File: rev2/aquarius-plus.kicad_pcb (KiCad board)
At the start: 2 copper layers, 167 x 115 mm, 173 parts, among them J1 Power in, J10 FPGA spare, J11 Hand controller 2, J12 Hand controller 1, J13 ESP32 spare, J2 ESP USB Host, J3 Audio out, J4 VGA, J5 Cassette out, J6 Cassette in, J7 Expansion port, J8 Printer, J9 TF-03A, Q1 BC847C, Q2 BC847C, Q3 2N7002, SW1 SW_DPDT_x2, U1 SN74AHCT1G125DBVR, U10 ESP32-S3-WROOM-1-N4R2, U11 LDL1117S33R, U12 SN74CB3T3245PWR, U13 IS61C5128AS-25QLI, U2 SN74AHCT1G125DBVR, U3 LD1117S12, U4 SN74CB3T3245PWR, U5 MAX3221ECPWR, U6 XC6SLX9-2TQG144C, U7 Z84C0010AEG, U8 SN74CB3T3245PWR, U9 SN74CB3T3245PWR, X1 SX3M14.31818M20F30TNN

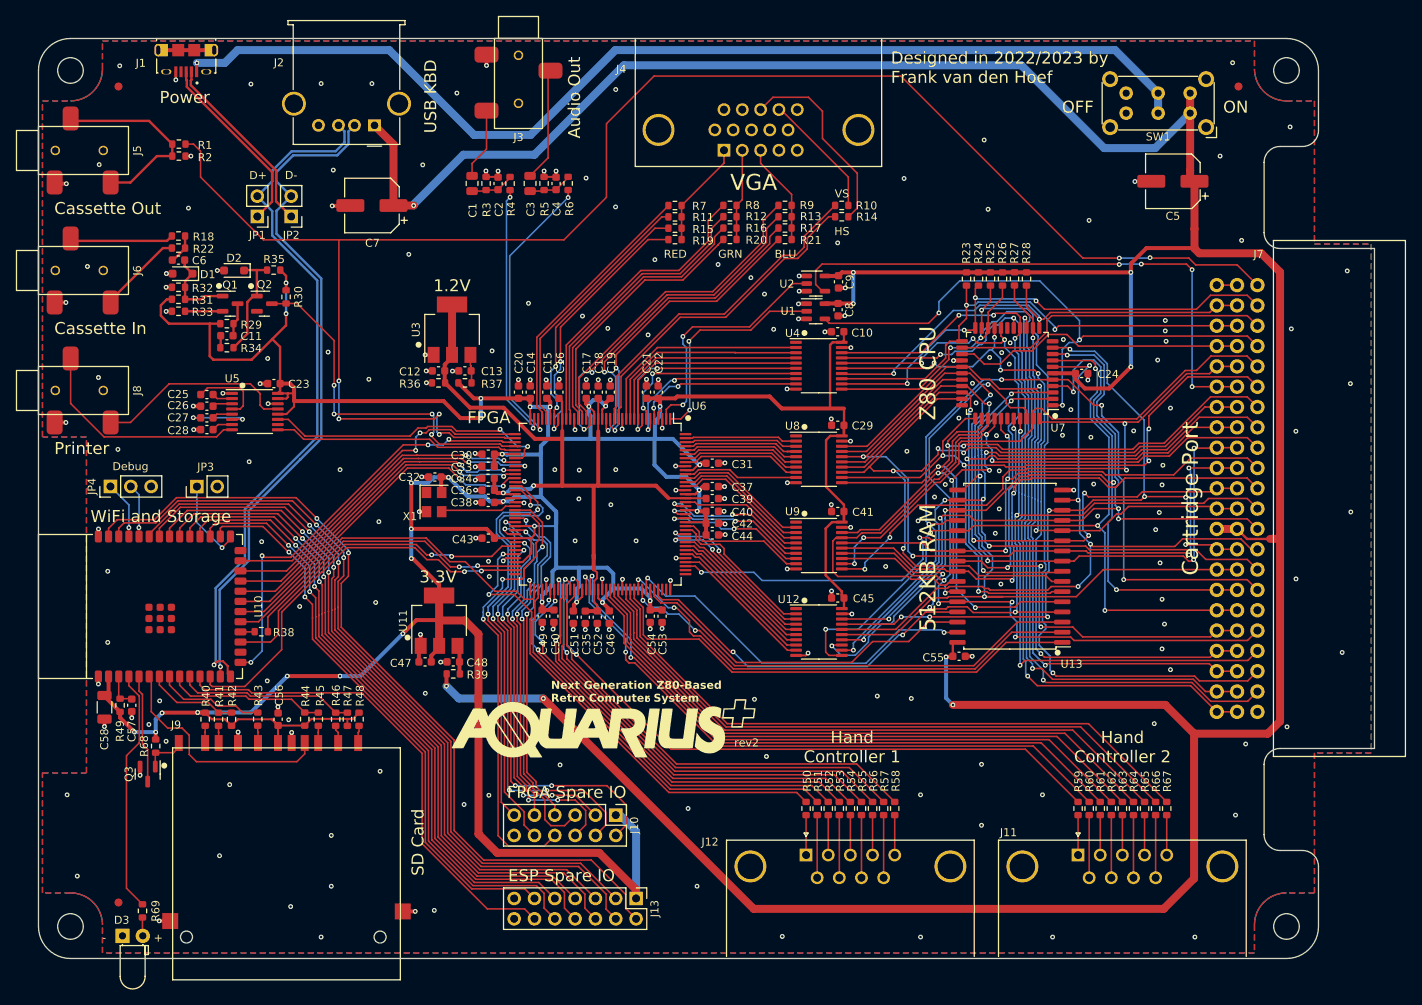
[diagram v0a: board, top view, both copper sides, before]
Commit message: PCB rev2-230718 Update to Use throughhole audio jacks (C2939180)
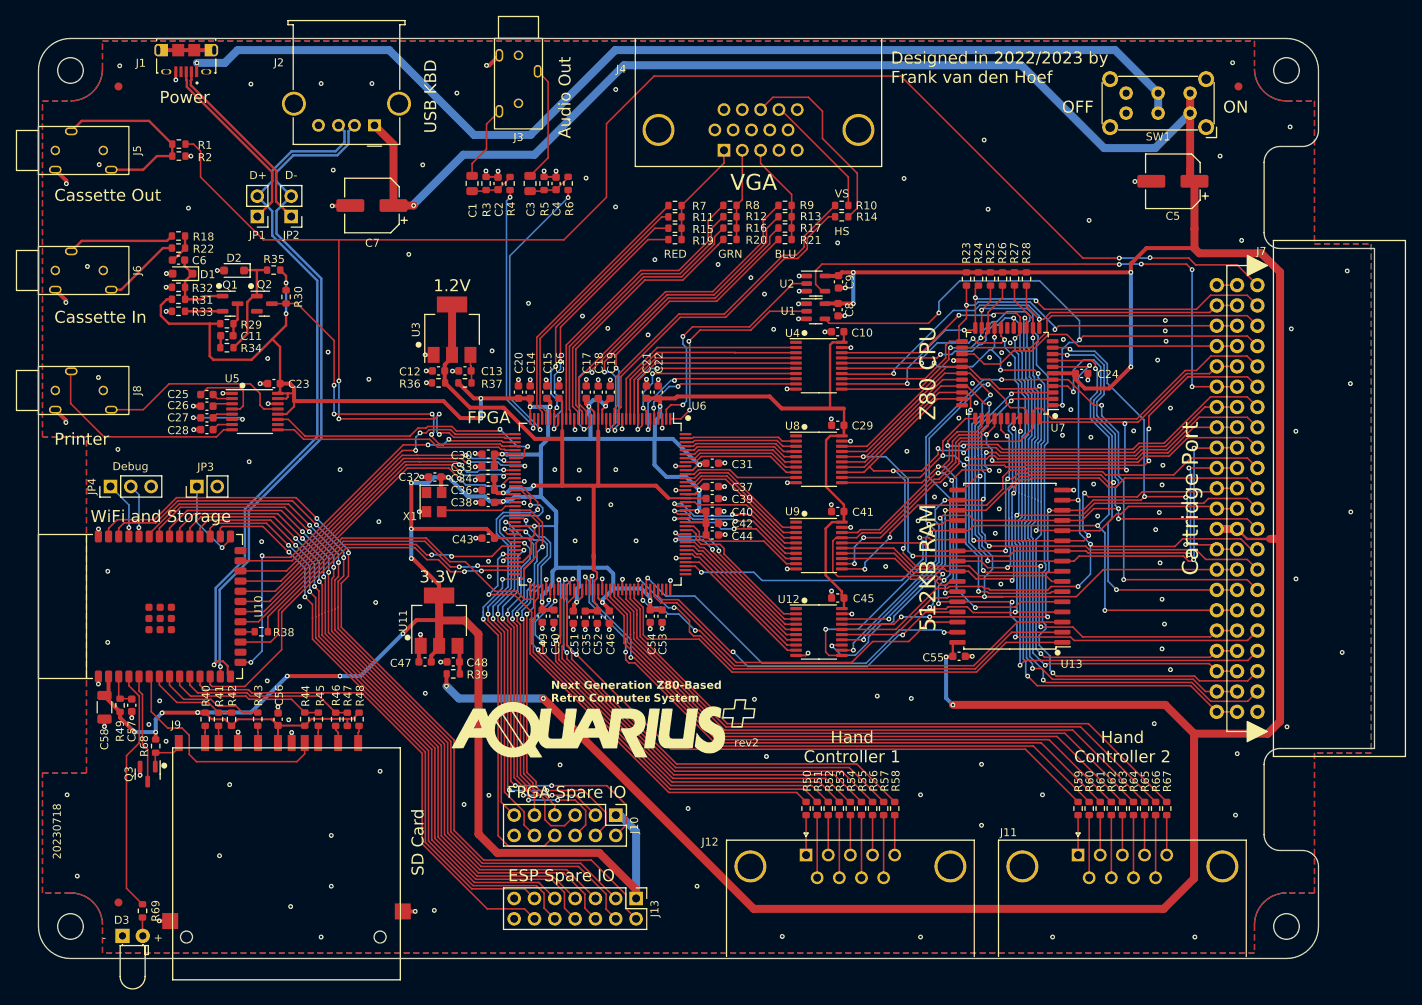
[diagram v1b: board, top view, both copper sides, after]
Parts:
- J3, J5, J6, J8: footprint aquarius-plus:C2884998 -> aquarius-plus:C2939180
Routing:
- net GND: track 115.7 -> 118.8 mm
- net Net-(U5-RIN): track 27.9 -> 26.3 mm
- net Net-(J6-PadT): track 10.6 -> 9.73 mm
- net Net-(U5-DOUT): track 25.1 -> 24.3 mm
- net Net-(C1-Pad2): track 8.88 -> 9.48 mm
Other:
- board text added: "20230718"
